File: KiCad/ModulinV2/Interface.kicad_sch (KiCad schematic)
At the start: 36 parts, among them IC2 ADS7041IDCUR, IC3 ADS7041IDCUR, IC4 ADS7866IDBVT, IC5 ADS7866IDBVT, IC6 DAC60501ZDGSR, IC7 DAC60501ZDGSR

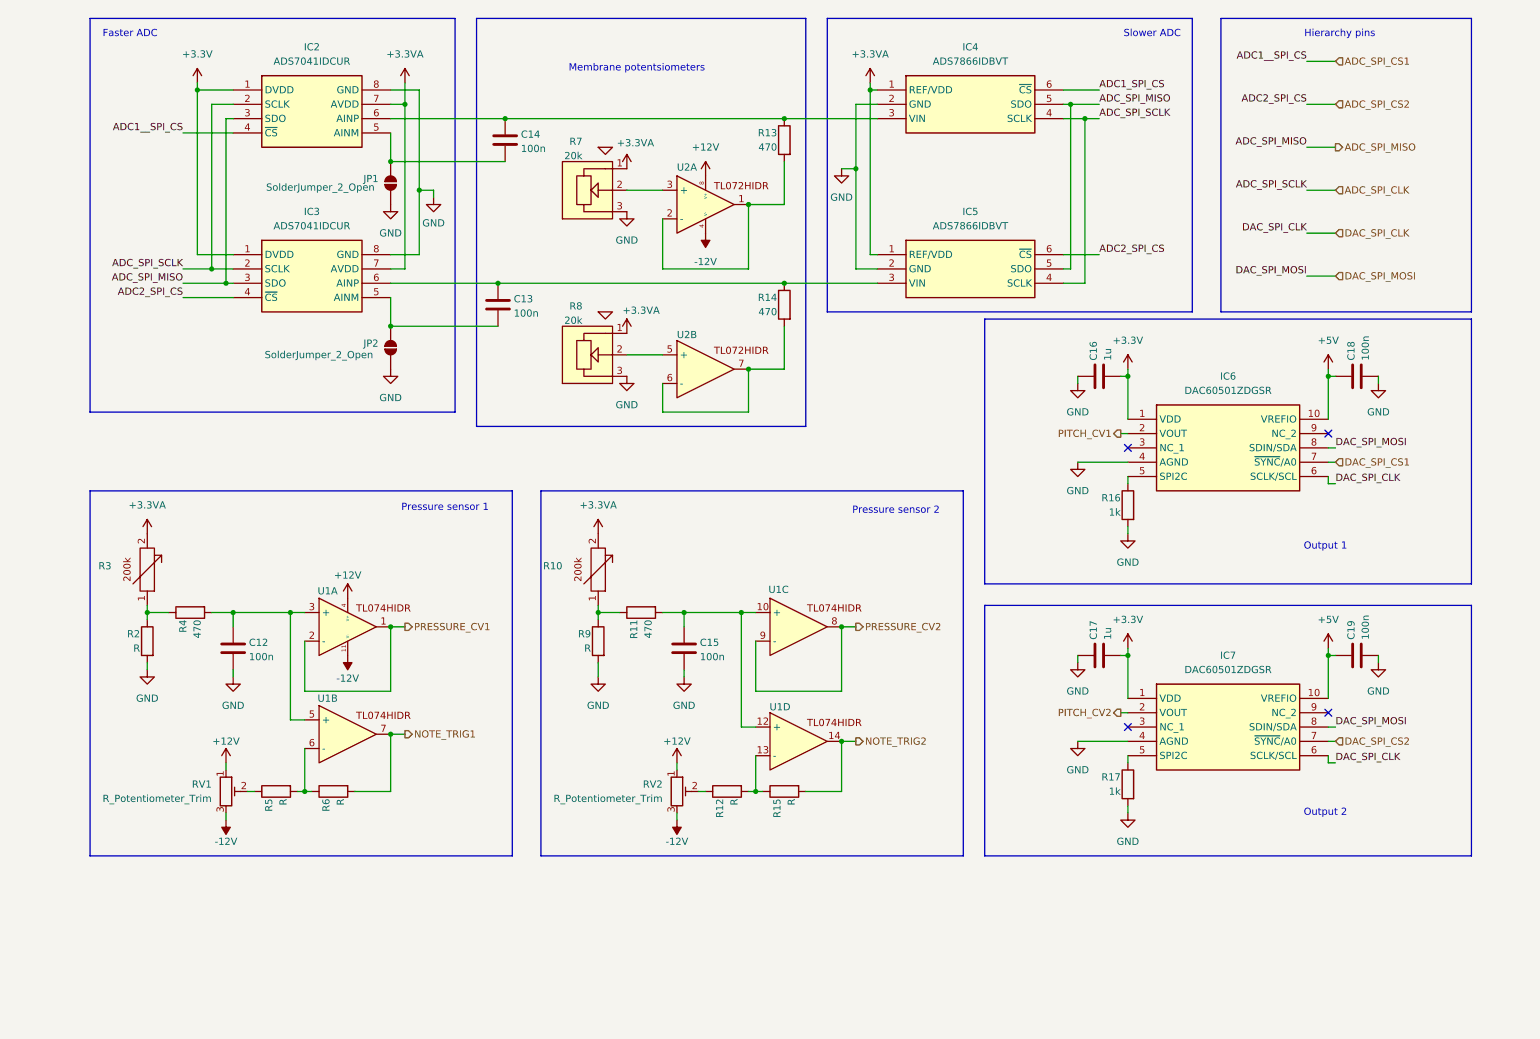
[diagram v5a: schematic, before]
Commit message: Modified USB connection and added LEDs
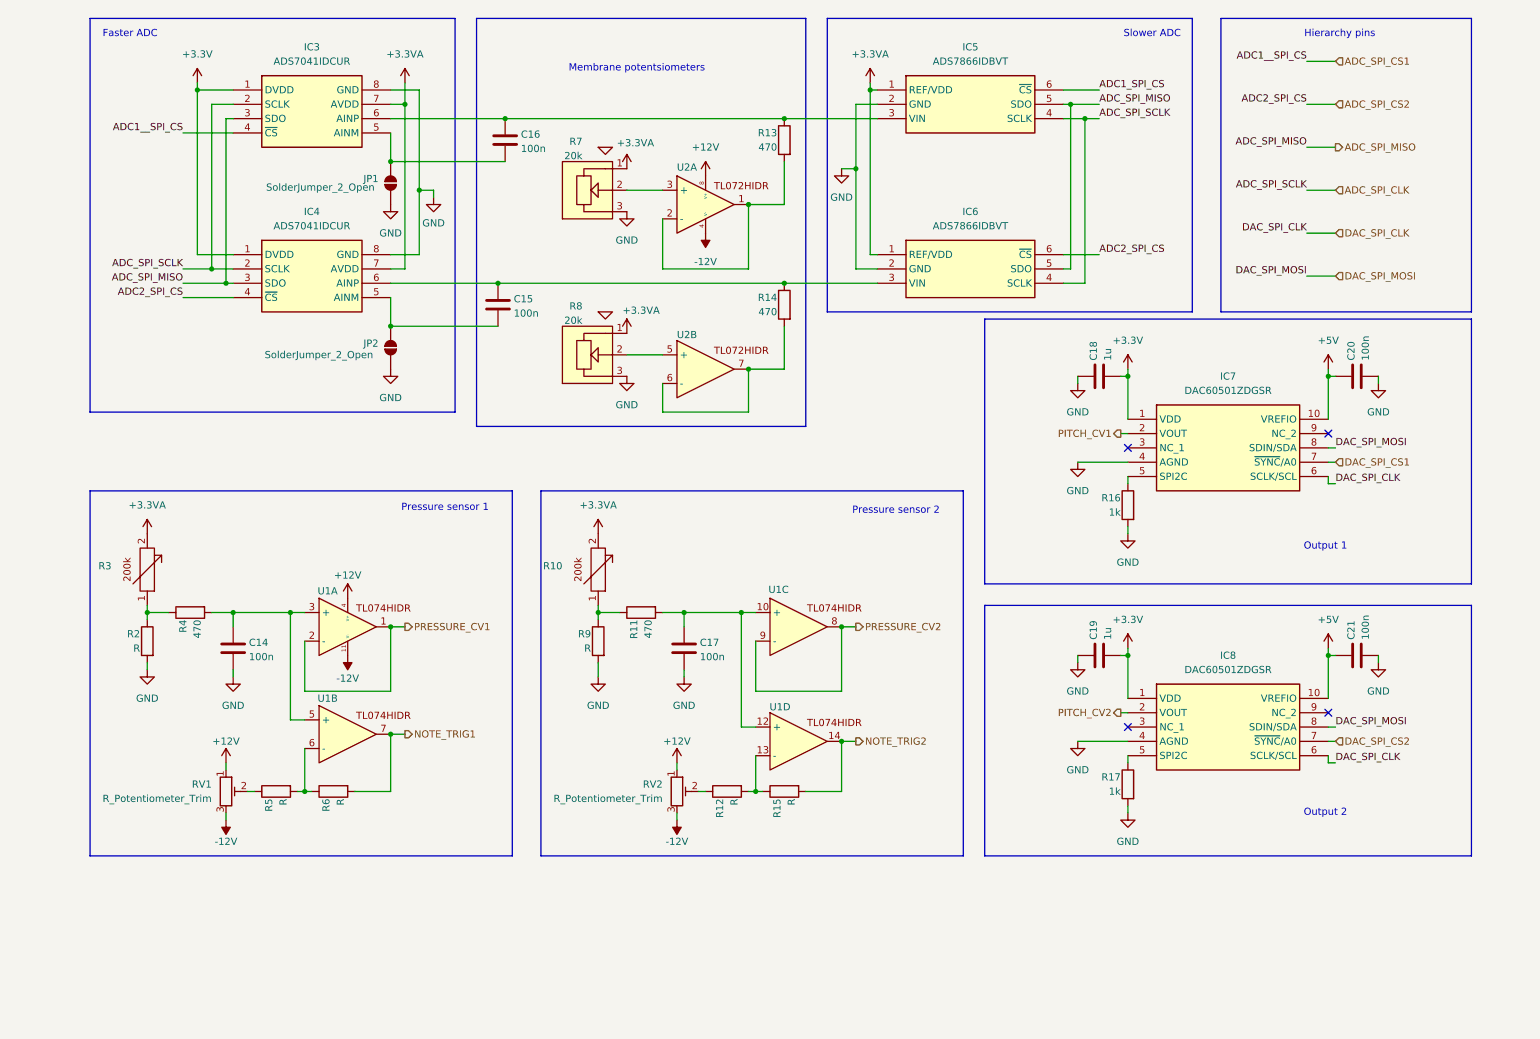
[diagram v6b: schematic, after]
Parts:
- renumbered C12 to C14, C13 to C15, C14 to C16, C15 to C17, C16 to C18, C17 to C19, C18 to C20, C19 to C21, IC2 to IC3, IC3 to IC4, IC4 to IC5, IC5 to IC6, IC6 to IC7, IC7 to IC8

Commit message: Fleshed out the waveform select schematic a bit + general cleanup
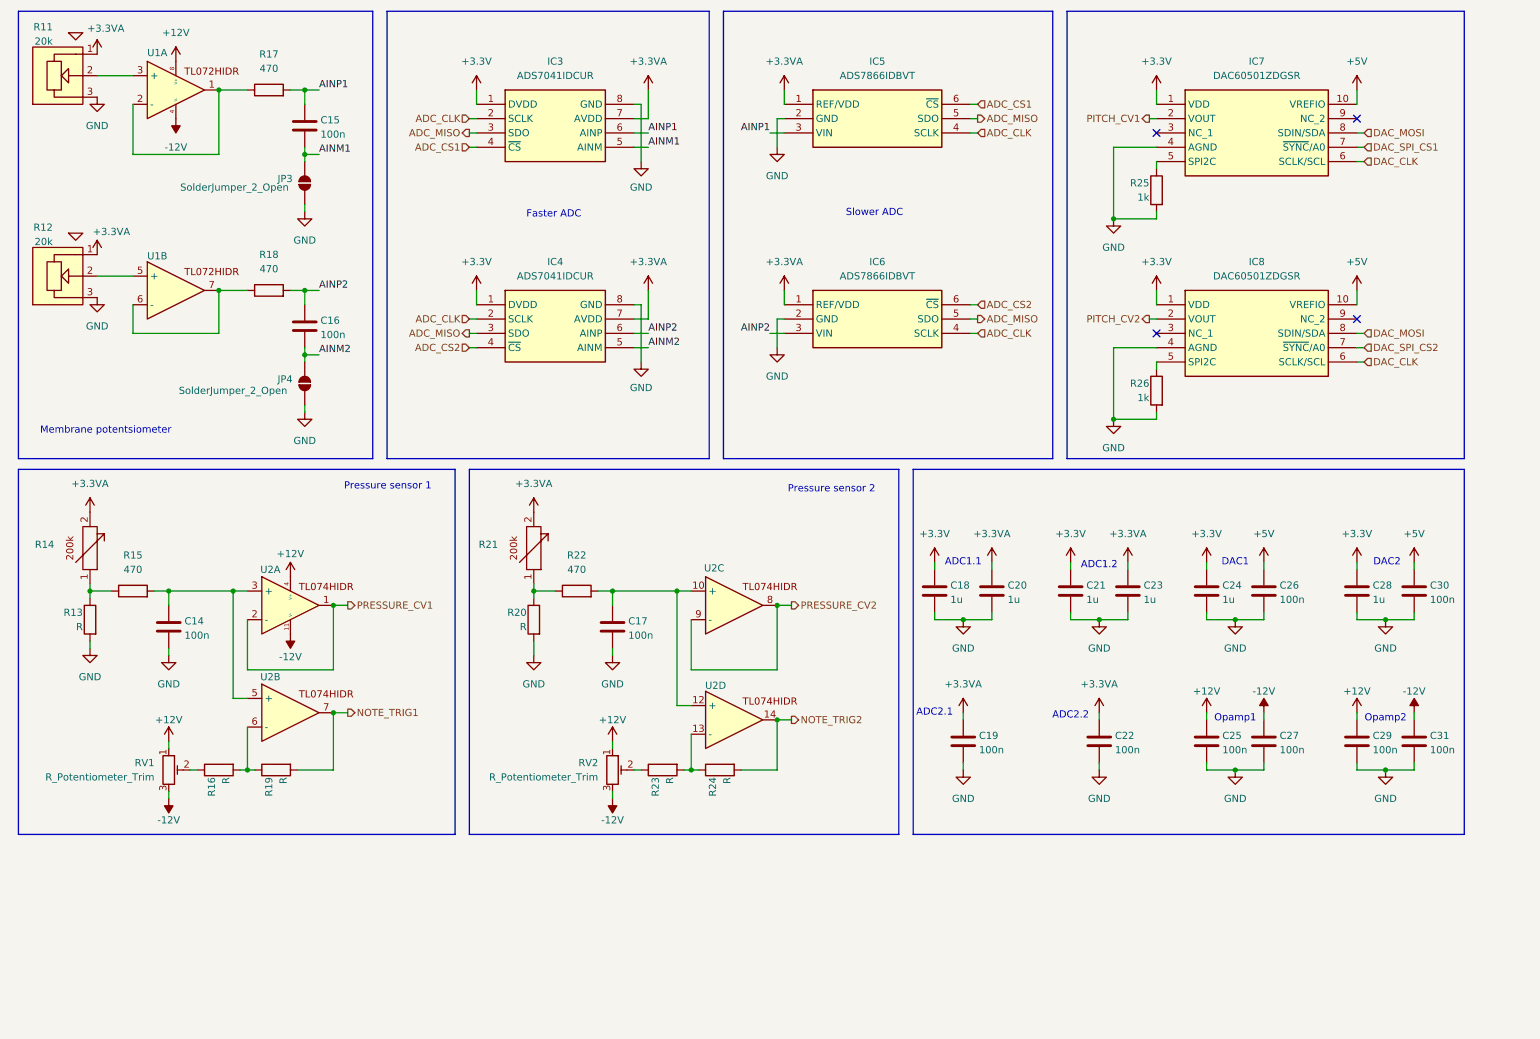
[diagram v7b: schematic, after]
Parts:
- removed R11, R13, R14, R4: 470, symbol Device:R
- added C18, C20, C23, C28: 1u, symbol Device:C
- added C22, C25, C27, C29, C30, C31: 100n, symbol Device:C
- added R15, R17, R18, R22: 470, symbol Device:R
- C19: value 1u -> 100n
- C21: value 100n -> 1u
- renumbered C16 to C15, C15 to C16, C18 to C24, C20 to C26, JP1 to JP3, JP2 to JP4, R7 to R11, R8 to R12, R2 to R13, R3 to R14, R5 to R16, R6 to R19, R9 to R20, R10 to R21, R12 to R23, R15 to R24, R16 to R25, R17 to R26, U2 to U1, U1 to U2
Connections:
- net ADC_SPI_CS1 is gone; now on net ADC_CS1: IC3.4 (~{CS})
- net +12V: now also C25.1, C29.1
- net +3.3V: now also C21.1, C24.1, C18.1, C28.1; no longer C19.2, C24.2
- net +3.3VA: now also C19.1, C20.1, C22.1, C23.1
- net +5V: now also C30.1; no longer C21.1
- net -12V: now also C27.1, C31.1
- net GND: now also C19.2, C24.2, C18.2, C20.2, C22.2, C23.2, C25.2, C27.2, C28.2, C29.2, C30.2, C31.2; no longer C19.1, C24.1
- net at R13.1, R14.1: now also R15.1
- net at R20.1, R21.1: now also R22.1
- net AINP1: now reaches C15.1, IC3.6 (AINP), IC5.3 (VIN)
- net AINP1: now also R17.2
- net at U1.1, U1.2 (-): now also R17.1
- net at C17.1, U2.10 (+), U2.12 (+): now also R22.2
- net AINP2: now reaches C16.1, IC4.6 (AINP), IC6.3 (VIN)
- net AINP2: now also R18.2
- net at U1.6 (-), U1.7: now also R18.1
- net at C14.1, U2.3 (+), U2.5 (+): now also R15.2
- net AINM1: now reaches C15.2, IC3.5 (AINM), JP3.2 (B)
- net AINM2: now reaches C16.2, IC4.5 (AINM), JP4.2 (B)
- net ADC1_SPI_CS renamed ADC_CS1
- net ADC_SPI_CLK renamed ADC_CLK
- net ADC_SPI_CS2 renamed ADC_CS2
- net ADC_SPI_MISO renamed ADC_MISO
- net DAC_SPI_CLK renamed DAC_CLK
- net DAC_SPI_MOSI renamed DAC_MOSI
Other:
- note added: "ADC1.1"
- note added: "ADC1.2"
- note added: "ADC2.1"
- note added: "ADC2.2"
- note added: "DAC1"
- note added: "DAC2"
- note added: "Membrane potentsiometer"
- note added: "Opamp1"
- note added: "Opamp2"
- note removed: "Hierarchy pins"
- note removed: "Membrane potentsiometers"
- note removed: "Output 1"
- note removed: "Output 2"
- moved on the sheet: C14, C15, C16, C17, C24, C26, IC3, IC4, IC5, IC6, IC7, IC8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

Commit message: Designed ADSR and better tuning schematics with digital/manual capability
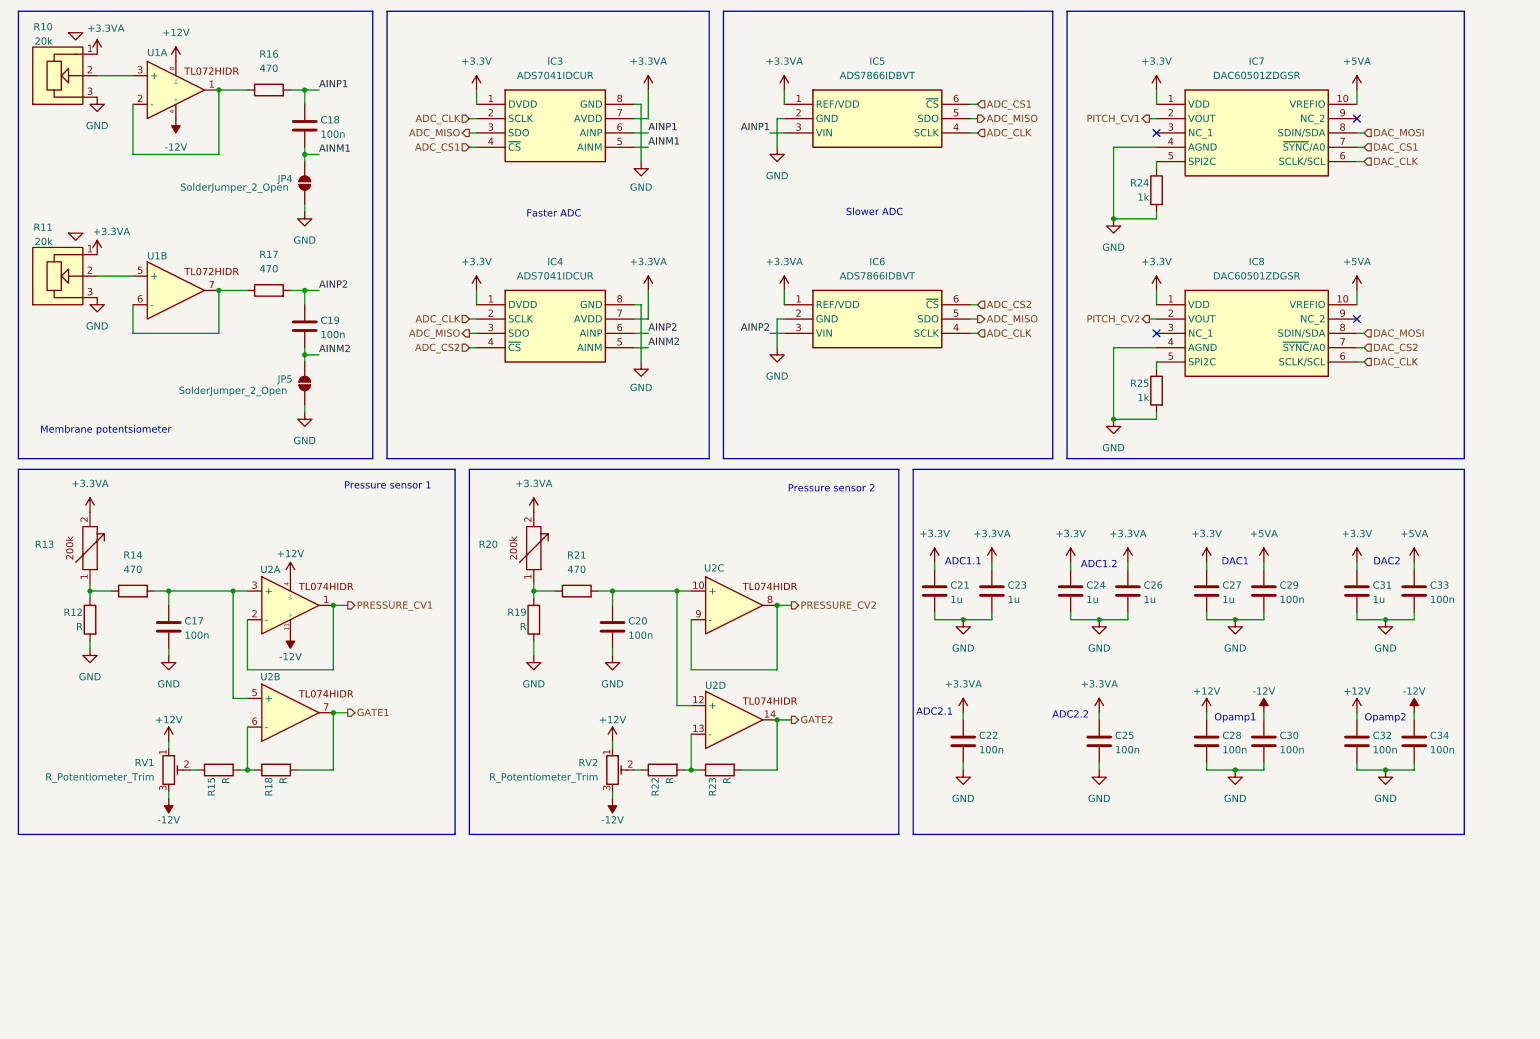
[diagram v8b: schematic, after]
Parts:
- renumbered C14 to C17, C15 to C18, C16 to C19, C17 to C20, C18 to C21, C19 to C22, C20 to C23, C21 to C24, C22 to C25, C23 to C26, C24 to C27, C25 to C28, C26 to C29, C27 to C30, C28 to C31, C29 to C32, C30 to C33, C31 to C34, JP3 to JP4, JP4 to JP5, R11 to R10, R12 to R11, R13 to R12, R14 to R13, R15 to R14, R16 to R15, R17 to R16, R18 to R17, R19 to R18, R20 to R19, R21 to R20, R22 to R21, R23 to R22, R24 to R23, R25 to R24, R26 to R25
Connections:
- net +5V renamed +5VA
- net DAC_SPI_CS1 renamed DAC_CS1
- net DAC_SPI_CS2 renamed DAC_CS2
- net NOTE_TRIG1 renamed GATE1
- net NOTE_TRIG2 renamed GATE2
